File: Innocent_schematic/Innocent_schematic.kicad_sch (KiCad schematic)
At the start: 35 parts, among them IC1 MP2338GTL-Z, P1 USB_C_Plug_USB2.0, U1 CH224K, U2 TP4056-42-ESOP8, U3 MP3423GG-Z, U4 RT6150AGQW

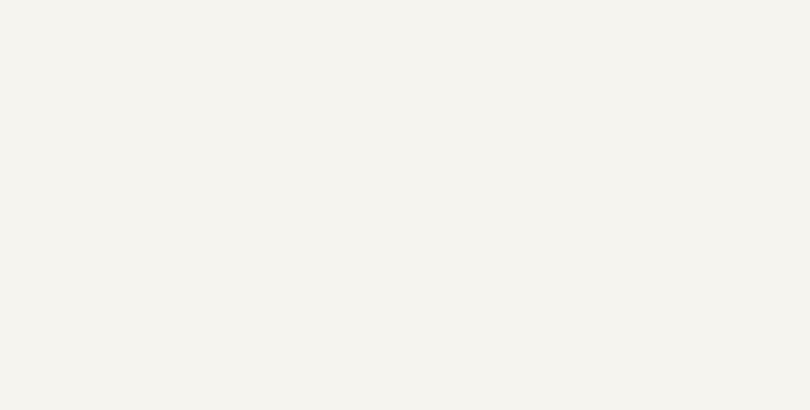
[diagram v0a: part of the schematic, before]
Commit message: i have added an IC2 to the schematic
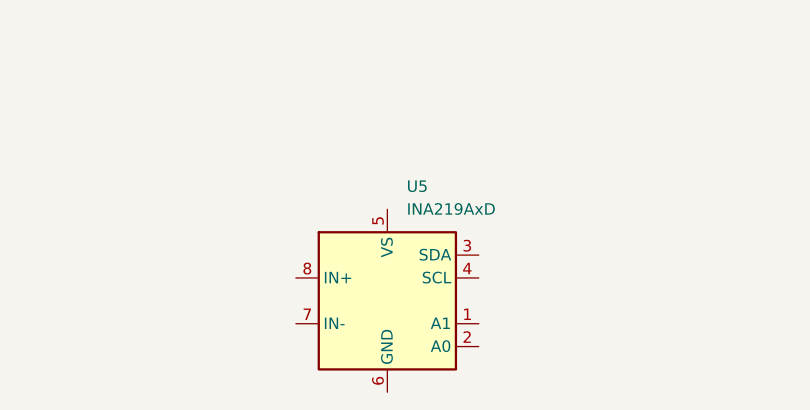
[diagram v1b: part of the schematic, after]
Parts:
- added U5: INA219AxD, Package_SO:SOIC-8_3.9x4.9mm_P1.27mm, symbol Sensor_Energy:INA219AxD
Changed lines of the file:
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@@
+	)
+	(symbol
+		(lib_id "Sensor_Energy:INA219AxD")
+		(at 83.82 176.53 0)
+		(unit 1)
+		(exclude_from_sim no)
+		(in_bom yes)
+		(on_board yes)
+		(dnp no)
+		(fields_autoplaced yes)
+		(property "Reference" "U5"
+			(at 85.9633 163.83 0)
+			(effects
+				(font
+					(size 1.27 1.27)
+				)
+				(justify left)
+			)
+		)
+		(property "Value" "INA219AxD"
+			(at 85.9633 166.37 0)
+			(effects
+				(font
+					(size 1.27 1.27)
+				)
+				(justify left)
+			)
+		)
+		(property "Footprint" "Package_SO:SOIC-8_3.9x4.9mm_P1.27mm"
+			(at 104.14 185.42 0)
+			(effects
+				(font
+					(size 1.27 1.27)
+				)
+				(hide yes)
+			)
+		)
+		(property "Datasheet" "http://www.ti.com/lit/ds/symlink/ina219.pdf"
+			(at 92.71 179.07 0)
+			(effects
+				(font
+					(size 1.27 1.27)
+				)
+				(hide yes)
+			)
+		)
+		(property "Description" "Zero-Drift, Bidirectional Current/Power Monitor (0-26V) With I2C Interface, SOIC-8"
+			(at 83.82 176.53 0)
+			(effects
+				(font
+					(size 1.27 1.27)
+				)
+				(hide yes)
+			)
+		)
+		(pin "7"
+		)
+		(pin "4"
+		)
+		(pin "6"
+		)
+		(pin "2"
+		)
+		(pin "5"
+		)
+		(pin "3"
+		)
+		(pin "1"
+		)
+		(pin "8"
+		)
+		(instances
+			(project ""
+				(path "/0ebc6b21-534b-4d26-a743-fadd30dffdd1"
+					(reference "U5")
+					(unit 1)
+				)
+			)
+		)
 	)
 	(symbol

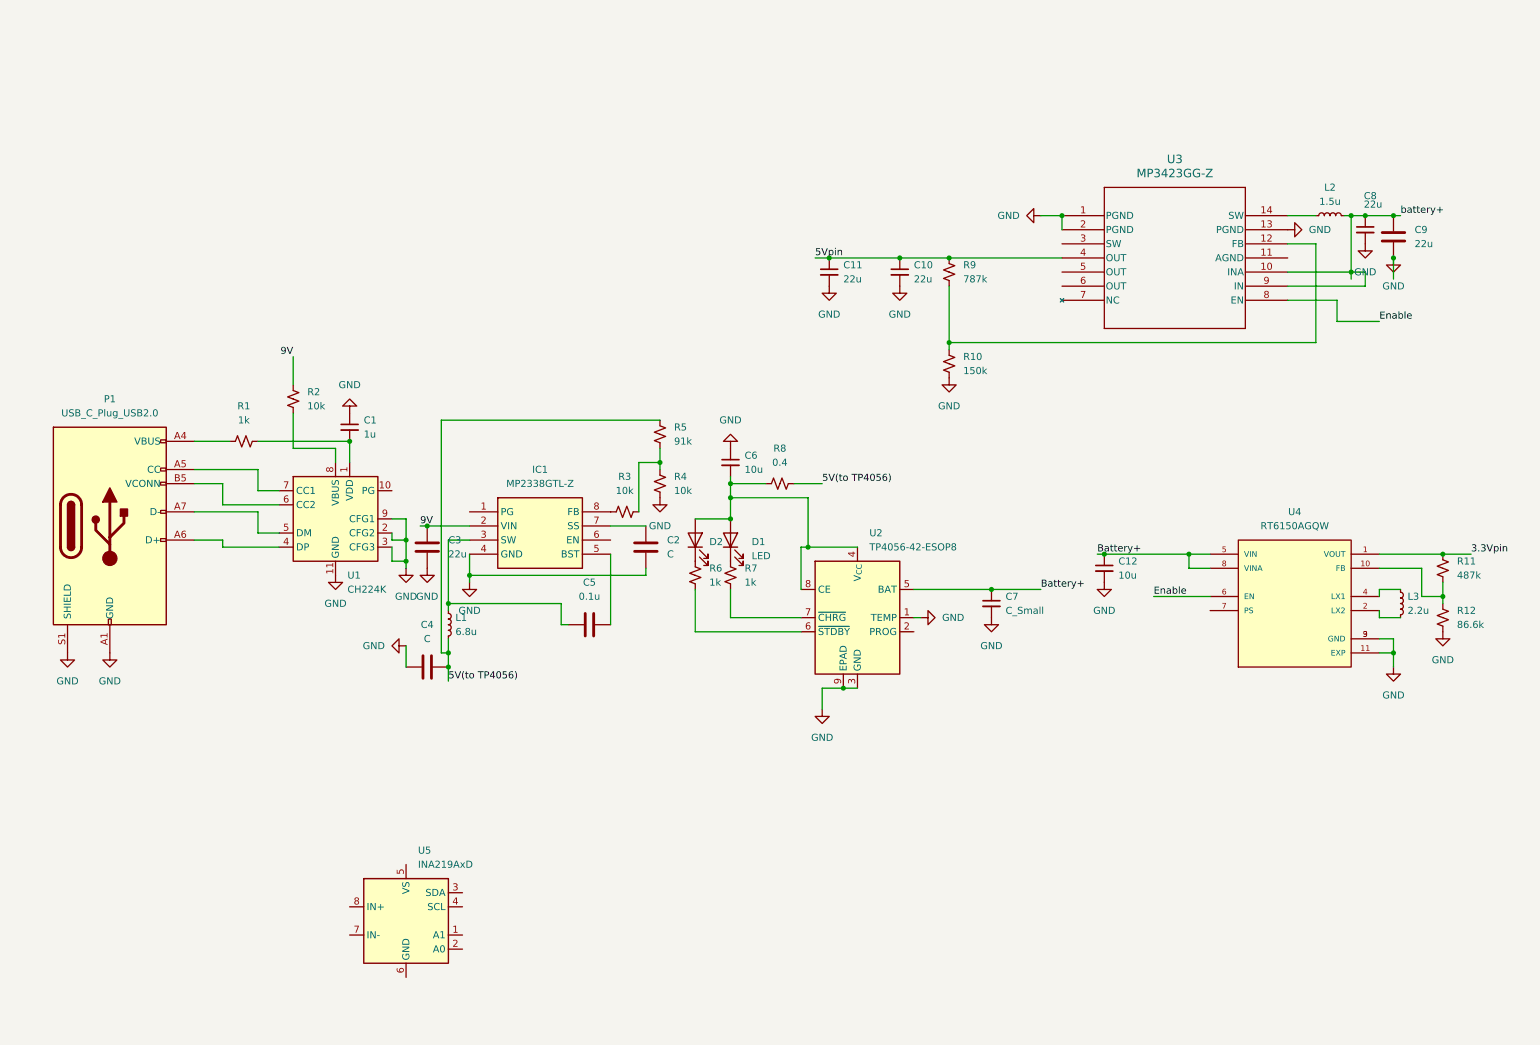
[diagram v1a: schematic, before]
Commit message: added TP4056,CH224K,MP2338,RT6150 AND MP3423 schematics and missing resistor values
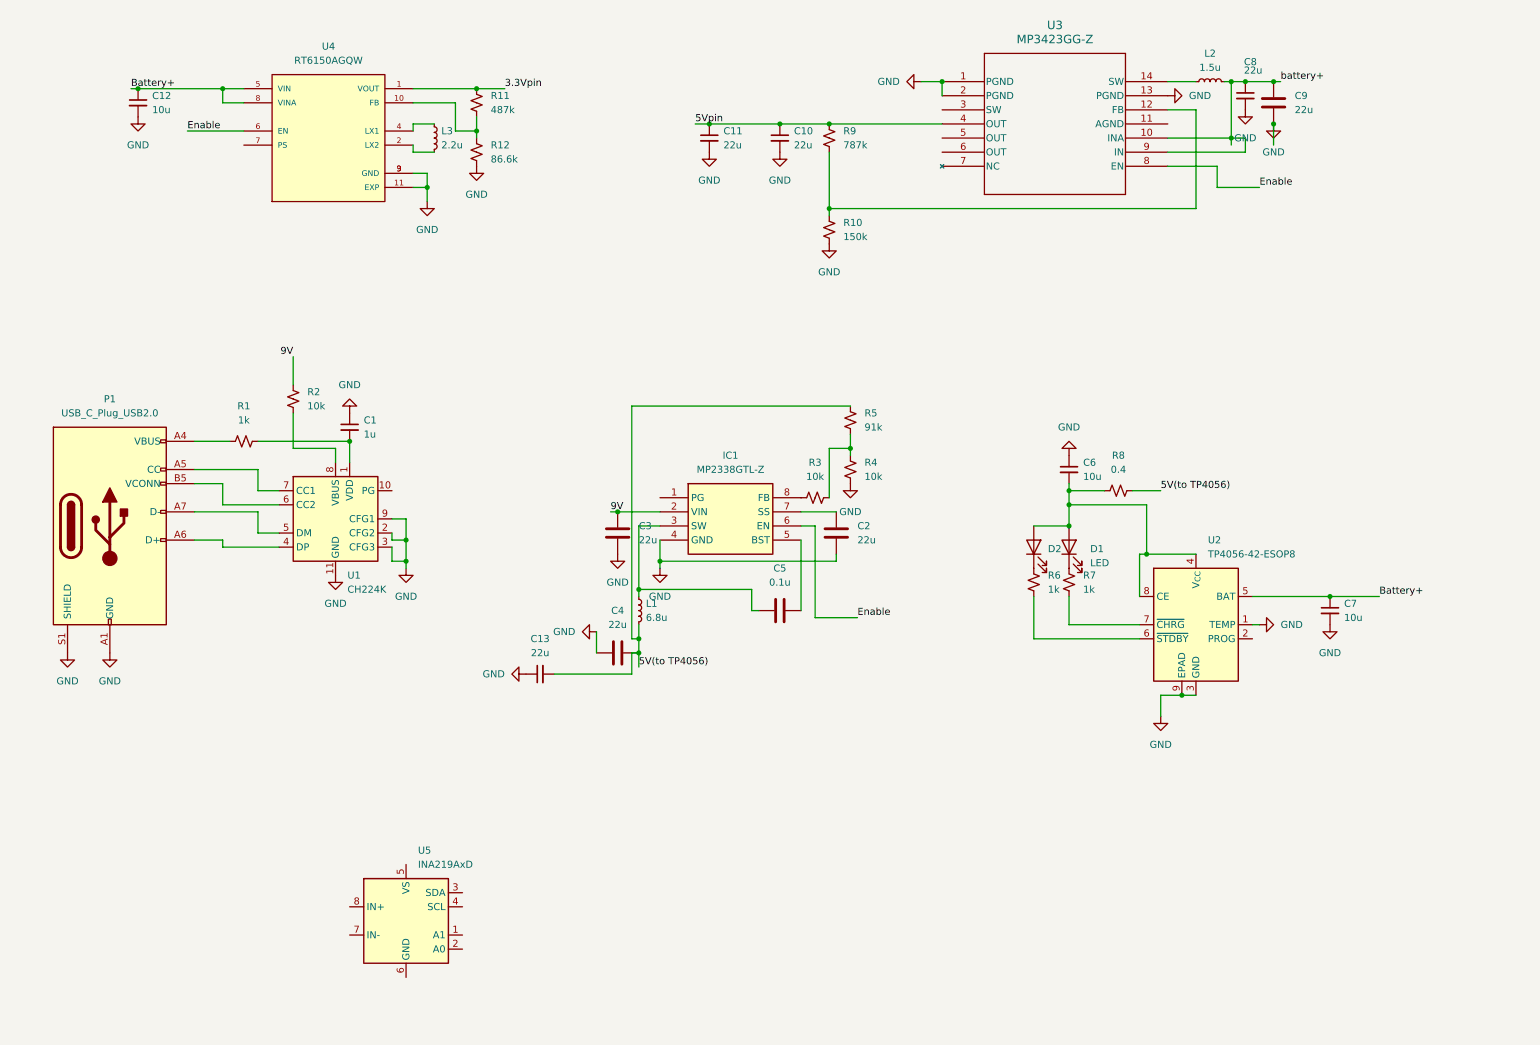
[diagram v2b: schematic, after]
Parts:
- added C13: 22u, symbol Device:C_Small
- C2, C4: value C -> 22u
- C7: value C_Small -> 10u
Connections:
- net 5V(to TP4056): now also C13.2
- net Enable: now also IC1.6 (EN)
- net GND: now also C13.1
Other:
- moved on the sheet: C10, C11, C12, C2, C3, C4, C5, C6, C7, C8, C9, D1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

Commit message: i have integrated all the systems into one project
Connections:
- net GND: no longer U2.1 (TEMP)
- net at C1.2, R1.2, U1.1 (VDD): now also R2.2, U1.8 (VBUS)
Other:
- moved on the sheet: C1, C10, C11, C12, C13, C2, C3, C4, C5, C6, C7, C8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

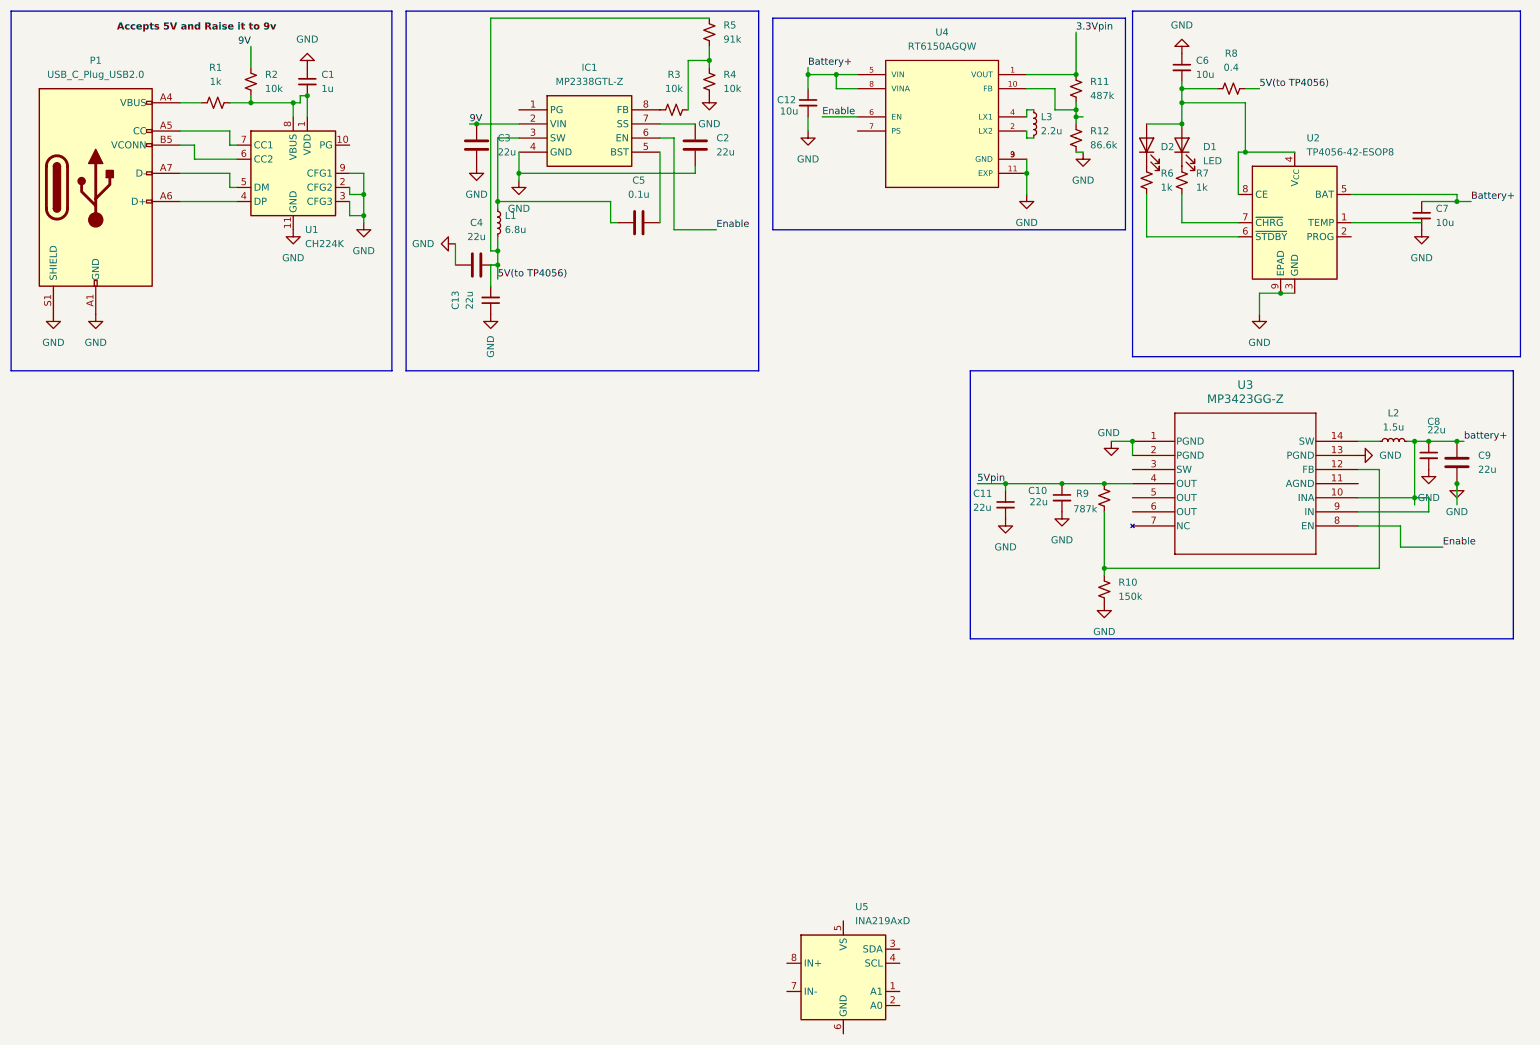
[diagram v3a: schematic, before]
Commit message: i have added the footprints to the folder and assigned most components, i am just left with JST pin and USB
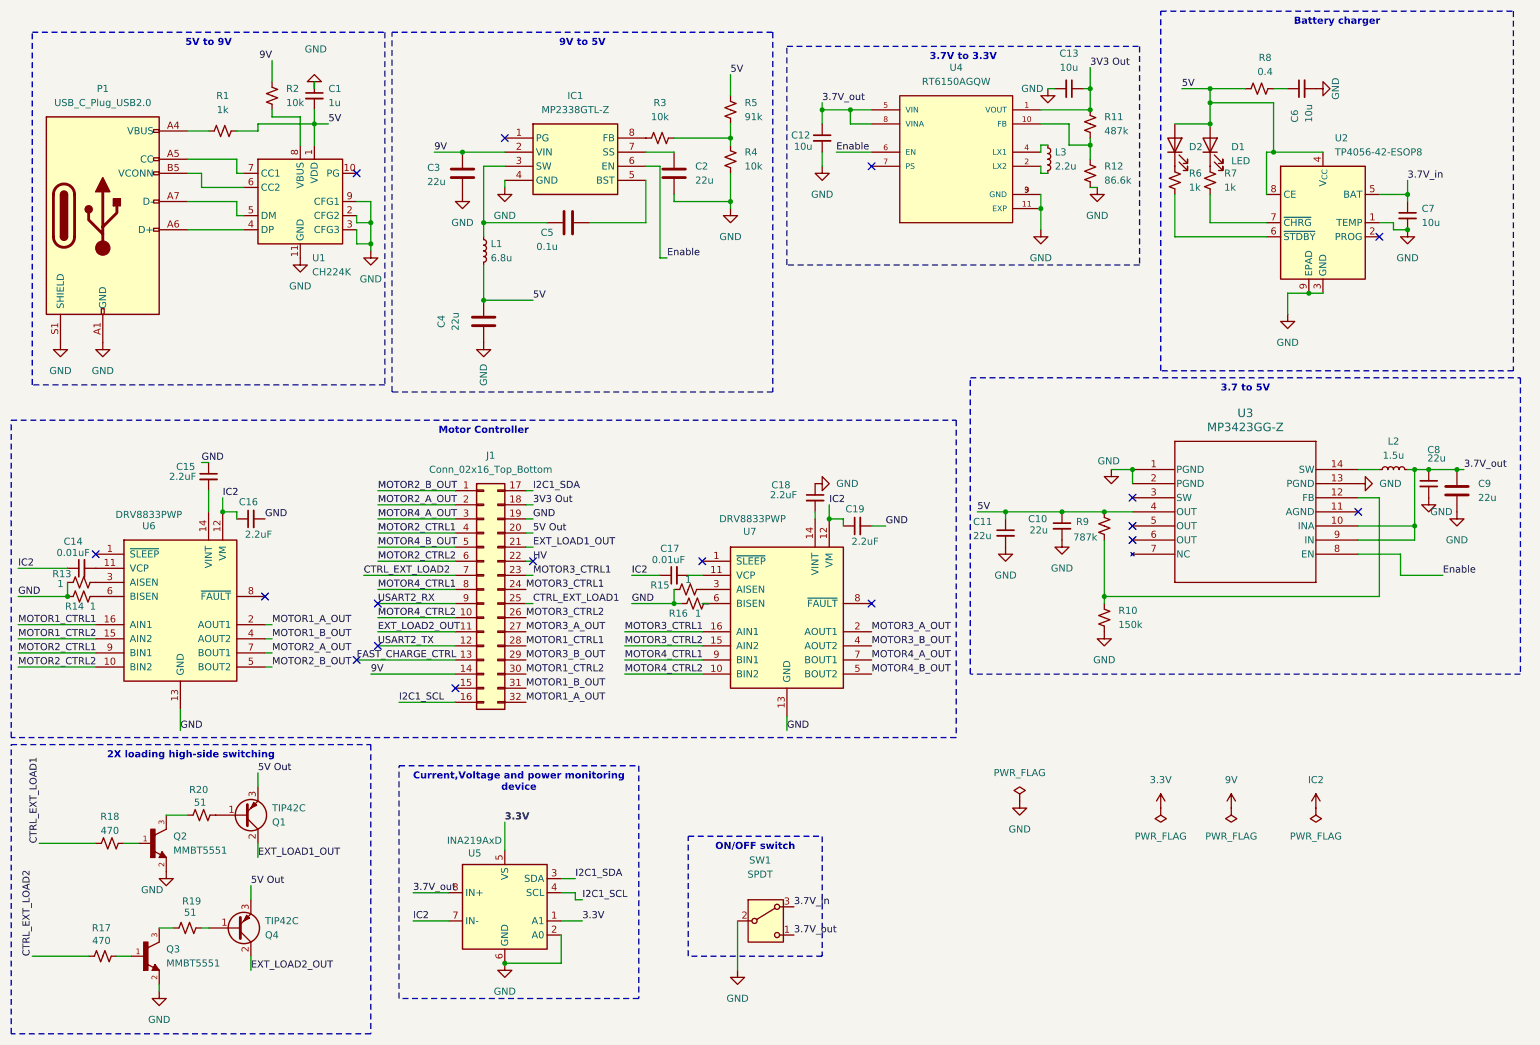
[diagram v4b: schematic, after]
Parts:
- added C14, C17: 0.01uF, Capacitor_SMD:C_0805_2012Metric, symbol Device:C_Small
- added C15, C16, C18, C19: 2.2uF, Capacitor_SMD:C_1206_3216Metric, symbol Device:C_Small
- added J1: Conn_02x16_Top_Bottom, Connector_PinHeader_2.54mm:PinHeader_2x16_P2.54mm_Vertical, symbol Connector_Generic:Conn_02x16_Top_Bottom
- added Q1, Q4: TIP42C, Package_TO_SOT_THT:TO-220-3_Vertical, symbol Transistor_BJT:TIP42C
- added Q2, Q3: MMBT5551, MMBT5551:SOT23-3, symbol MMBT5551:MMBT5551
- added R13, R14, R15, R16: 1, Resistor_SMD:R_1206_3216Metric, symbol Device:R_Small_US
- added R17, R18: 470, Resistor_SMD:R_0805_2012Metric, symbol Device:R_Small_US
- added R19, R20: 51, Resistor_SMD:R_0805_2012Metric, symbol Device:R_Small_US
- added SW1: SPDT, MyLibrary:NEWSWITCH, symbol Switch:SW_Nidec_CAS-120A1
- added U6, U7: DRV8833PWP, Package_SO:HTSSOP-16-1EP_4.4x5mm_P0.65mm_EP3.4x5mm_Mask2.46x2.31mm_ThermalVias, symbol Driver_Motor:DRV8833PWP
- C1: footprint (none) -> Capacitor_SMD:C_0402_1005Metric
- C10, C11, C2, C3, C4, C8, C9: footprint (none) -> Capacitor_SMD:C_1206_3216Metric
- C12, C6, C7: footprint (none) -> Capacitor_SMD:C_0805_2012Metric
- C13: value 22u -> 10u; footprint (none) -> Capacitor_SMD:C_0805_2012Metric
- C5: footprint (none) -> Capacitor_SMD:C_0603_1608Metric
- D1, D2: footprint (none) -> LED_SMD:LED_0805_2012Metric
- IC1: footprint MP2338GTLZ -> MP2338GTL-Z:MP2338GTLZ
- L1: footprint (none) -> Inductor_SMD:L_1008_2520Metric
- L2: footprint (none) -> Inductor_SMD:L_0805_2012Metric
- L3: footprint (none) -> Inductor_SMD:L_1210_3225Metric
- P1: footprint (none) -> Connector_USB:USB_C_Receptacle_GCT_USB4125-xx-x-0190_6P_TopMnt_Horizontal
- R1, R10, R12, R2, R3, R4, R5, R6, R7, R8: footprint (none) -> Resistor_SMD:R_0805_2012Metric
- R11: footprint (none) -> Resistor_SMD:R_0402_1005Metric
- R9: footprint (none) -> Resistor_SMD:R_0603_1608Metric
- U3: footprint QFN14_MP3423_MNP -> ul_MP3423GG-Z:QFN14_MP3423_MNP-L
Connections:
- net 5Vpin is gone; now on net 5V: C10.1, C11.1, R9.2, U3.4 (OUT)
- net battery+ is gone; now on net 3.7V_out: C8.1, C9.1, L2.2, U3.10 (INA), U3.9 (IN)
- net 9V: now also J1.14 (Pin_14)
- net GND: now also C13.2, C6.2, U2.1 (TEMP), U5.2 (A0), U5.6 (GND), C15.1, C16.2, C18.1, C19.2, J1.19 (Pin_19), Q2.2, Q3.2, R13.1, R14.1, R15.1, R16.1, SW1.2 (B), U6.13 (GND), U6.17 (GND), U7.13 (GND), U7.17 (GND); no longer C13.1, C6.1
- net 5V: now reaches C1.2, R1.2, U1.1 (VDD)
- net 5V: now also C4.2, D1.2 (A), D2.2 (A), L1.2, R5.1, R8.2, U2.4 (V_{CC}), U2.8 (CE); no longer R2.2, U1.8 (VBUS)
- net 3.3V: now reaches U5.1 (A1)
- net 3.3V: now also U5.5 (VS)
- net I2C1_SDA: now reaches U5.3 (SDA)
- net I2C1_SDA: now also J1.17 (Pin_17)
- net I2C1_SCL: now reaches U5.4 (SCL)
- net I2C1_SCL: now also J1.16 (Pin_16)
- net IC2: now reaches U5.7 (IN-)
- net IC2: now also C14.1, C16.1, C17.1, C19.1, U6.12 (VM), U7.12 (VM)
- net 3.7V_out: now reaches U5.8 (IN+)
- net 3.7V_out: now also C12.1, U4.5 (VIN), U4.8 (VINA), SW1.1 (C)
- net 3.3Vpin renamed 3V3 Out
- net 3V3 Out: now also C13.1, J1.18 (Pin_18)
- removed net 5V(to TP4056): C13.2, C4.2, L1.2, R5.1, R8.1
- removed net Battery+: C12.1, C7.1, U2.5 (BAT), U4.5 (VIN), U4.8 (VINA)
- new net: Q3.1, R17.2
- new net: Q3.3, R19.1
- new net: R2.2, U1.8 (VBUS)
- new net: Q2.3, R20.1
- new net: Q1.1 (B), R20.2
- new net: C18.2, U7.14 (VINT)
- new net: R15.2, U7.3 (AISEN)
- new net: R14.2, U6.6 (BISEN)
- new net: Q4.1 (B), R19.2
- new net: C14.2, U6.11 (VCP)
- new net: C15.2, U6.14 (VINT)
- new net: R13.2, U6.3 (AISEN)
- new net: Q2.1, R18.2
- new net: C17.2, U7.11 (VCP)
- new net: R16.2, U7.6 (BISEN)
- new net: C6.1, R8.1
- new net 3.7V_in: C7.1, SW1.3 (A), U2.5 (BAT)
- new net 5V Out: J1.20 (Pin_20), Q1.3 (E), Q4.3 (E)
- new net CTRL_EXT_LOAD1: J1.25 (Pin_25), R18.1
- new net CTRL_EXT_LOAD2: J1.7 (Pin_7), R17.1
- new net EXT_LOAD1_OUT: J1.21 (Pin_21), Q1.2 (C)
- new net EXT_LOAD2_OUT: J1.11 (Pin_11), Q4.2 (C)
- new net FAST_CHARGE_CTRL: J1.13 (Pin_13)
- new net HV: J1.22 (Pin_22)
- new net MOTOR1_A_OUT: J1.32 (Pin_32), U6.2 (AOUT1)
- new net MOTOR1_B_OUT: J1.31 (Pin_31), U6.4 (AOUT2)
- new net MOTOR1_CTRL1: J1.28 (Pin_28), U6.16 (AIN1)
- new net MOTOR1_CTRL2: J1.30 (Pin_30), U6.15 (AIN2)
- new net MOTOR2_A_OUT: J1.2 (Pin_2), U6.7 (BOUT1)
- new net MOTOR2_B_OUT: J1.1 (Pin_1), U6.5 (BOUT2)
- new net MOTOR2_CTRL1: J1.4 (Pin_4), U6.9 (BIN1)
- new net MOTOR2_CTRL2: J1.6 (Pin_6), U6.10 (BIN2)
- new net MOTOR3_A_OUT: J1.27 (Pin_27), U7.2 (AOUT1)
- new net MOTOR3_B_OUT: J1.29 (Pin_29), U7.4 (AOUT2)
- new net MOTOR3_CTRL1: J1.23 (Pin_23), J1.24 (Pin_24), U7.16 (AIN1)
- new net MOTOR3_CTRL2: J1.26 (Pin_26), U7.15 (AIN2)
- new net MOTOR4_A_OUT: J1.3 (Pin_3), U7.7 (BOUT1)
- new net MOTOR4_B_OUT: J1.5 (Pin_5), U7.5 (BOUT2)
- new net MOTOR4_CTRL1: J1.8 (Pin_8), U7.9 (BIN1)
- new net MOTOR4_CTRL2: J1.10 (Pin_10), U7.10 (BIN2)
- new net USART2_RX: J1.9 (Pin_9)
- new net USART2_TX: J1.12 (Pin_12)
- no-connect marks 0 -> 17
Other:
- company: (none) -> University of Cape Town
- title: (none) -> EEE3088F_Micromouse_power_module
- moved on the sheet: C1, C10, C11, C12, C2, C3, C4, C5, C6, C7, C8, C9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
